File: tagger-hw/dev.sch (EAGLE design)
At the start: 50 parts, among them J2 22-23-2021, J3 22-23-2021, X1 EXC-31B

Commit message: Fix some package sizes (0805 -> 0603)
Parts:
- ACT, PGOOD, USBACT: device adafruit:LEDCHIP-LED0805 -> adafruit:LEDCHIP-LED0603
- R1, R12, R13: device adafruit:R-US_R0805 -> adafruit:R-US_R0603
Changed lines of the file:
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@@
 <grid distance="0.1" unitdist="inch" unit="inch" style="lines" multiple="1" display="no" altdistance="0.01" altunitdist="inch" altunit="inch"/>
 <layers>
-<layer number="1" name="Top" color="4" fill="1" visible="no" active="no"/>
-<layer number="16" name="Bottom" color="1" fill="1" visible="no" active="no"/>
-<layer number="17" name="Pads" color="2" fill="1" visible="no" active="no"/>
-<layer number="18" name="Vias" color="2" fill="1" visible="no" active="no"/>
-<layer number="19" name="Unrouted" color="6" fill="1" visible="no" active="no"/>
-<layer number="20" name="Dimension" color="24" fill="1" visible="no" active="no"/>
-<layer number="21" name="tPlace" color="7" fill="1" visible="no" active="no"/>
-<layer number="22" name="bPlace" color="7" fill="1" visible="no" active="no"/>
-<layer number="23" name="tOrigins" color="15" fill="1" visible="no" active="no"/>
-<layer number="24" name="bOrigins" color="15" fill="1" visible="no" active="no"/>
-<layer number="25" name="tNames" color="7" fill="1" visible="no" active="no"/>
-<layer number="26" name="bNames" color="7" fill="1" visible="no" active="no"/>
-<layer number="27" name="tValues" color="7" fill="1" visible="no" active="no"/>
-<layer number="28" name="bValues" color="7" fill="1" visible="no" active="no"/>
+<layer number="1" name="Top" color="4" fill="1" visible="yes" active="no"/>
+<layer number="16" name="Bottom" color="1" fill="1" visible="yes" active="no"/>
+<layer number="17" name="Pads" color="2" fill="1" visible="yes" active="no"/>
+<layer number="18" name="Vias" color="2" fill="1" visible="yes" active="no"/>
+<layer number="19" name="Unrouted" color="6" fill="1" visible="yes" active="no"/>
+<layer number="20" name="Dimension" color="24" fill="1" visible="yes" active="no"/>
+<layer number="21" name="tPlace" color="7" fill="1" visible="yes" active="no"/>
+<layer number="22" name="bPlace" color="7" fill="1" visible="yes" active="no"/>
+<layer number="23" name="tOrigins" color="15" fill="1" visible="yes" active="no"/>
+<layer number="24" name="bOrigins" color="15" fill="1" visible="yes" active="no"/>
+<layer number="25" name="tNames" color="7" fill="1" visible="yes" active="no"/>
+<layer number="26" name="bNames" color="7" fill="1" visible="yes" active="no"/>
+<layer number="27" name="tValues" color="7" fill="1" visible="yes" active="no"/>
+<layer number="28" name="bValues" color="7" fill="1" visible="yes" active="no"/>
 <layer number="29" name="tStop" color="7" fill="3" visible="no" active="no"/>
 <layer number="30" name="bStop" color="7" fill="6" visible="no" active="no"/>
@@
 <layer number="35" name="tGlue" color="7" fill="4" visible="no" active="no"/>
 <layer number="36" name="bGlue" color="7" fill="5" visible="no" active="no"/>
-<layer number="37" name="tTest" color="7" fill="1" visible="no" active="no"/>
-<layer number="38" name="bTest" color="7" fill="1" visible="no" active="no"/>
+<layer number="37" name="tTest" color="7" fill="1" visible="yes" active="no"/>
+<layer number="38" name="bTest" color="7" fill="1" visible="yes" active="no"/>
 <layer number="39" name="tKeepout" color="4" fill="11" visible="no" active="no"/>
 <layer number="40" name="bKeepout" color="1" fill="11" visible="no" active="no"/>
@@
 <layer number="44" name="Drills" color="7" fill="1" visible="no" active="no"/>
 <layer number="45" name="Holes" color="7" fill="1" visible="no" active="no"/>
-<layer number="46" name="Milling" color="3" fill="1" visible="no" active="no"/>
-<layer number="47" name="Measures" color="7" fill="1" visible="no" active="no"/>
-<layer number="48" name="Document" color="7" fill="1" visible="no" active="no"/>
-<layer number="49" name="Reference" color="7" fill="1" visible="no" active="no"/>
-<layer number="50" name="dxf" color="7" fill="1" visible="no" active="no"/>
-<layer number="51" name="tDocu" color="7" fill="1" visible="no" active="no"/>
-<layer number="52" name="bDocu" color="7" fill="1" visible="no" active="no"/>
-<layer number="53" name="tGND_GNDA" color="7" fill="9" visible="no" active="no"/>
-<layer number="54" name="bGND_GNDA" color="1" fill="9" visible="no" active="no"/>
-<layer number="56" name="wert" color="7" fill="1" visible="no" active="no"/>
-<layer number="57" name="tCAD" color="7" fill="1" visible="no" active="no"/>
-<layer number="59" name="tCarbon" color="7" fill="1" visible="no" active="no"/>
-<layer number="60" name="bCarbon" color="7" fill="1" visible="no" active="no"/>
+<layer number="46" name="Milling" color="3" fill="1" visible="yes" active="no"/>
+<layer number="47" name="Measures" color="7" fill="1" visible="yes" active="no"/>
+<layer number="48" name="Document" color="7" fill="1" visible="yes" active="no"/>
+<layer number="49" name="Reference" color="7" fill="1" visible="yes" active="no"/>
+<layer number="50" name="dxf" color="7" fill="1" visible="yes" active="no"/>
+<layer number="51" name="tDocu" color="7" fill="1" visible="yes" active="no"/>
+<layer number="52" name="bDocu" color="7" fill="1" visible="yes" active="no"/>
+<layer number="53" name="tGND_GNDA" color="7" fill="9" visible="yes" active="no"/>
+<layer number="54" name="bGND_GNDA" color="1" fill="9" visible="yes" active="no"/>
+<layer number="56" name="wert" color="7" fill="1" visible="yes" active="no"/>
+<layer number="57" name="tCAD" color="7" fill="1" visible="yes" active="no"/>
+<layer number="59" name="tCarbon" color="7" fill="1" visible="yes" active="no"/>
+<layer number="60" name="bCarbon" color="7" fill="1" visible="yes" active="no"/>
 <layer number="88" name="SimResults" color="9" fill="1" visible="yes" active="yes"/>
 <layer number="89" name="SimProbes" color="9" fill="1" visible="yes" active="yes"/>
@@
 <part name="SUPPLY4" library="supply2" library_urn="urn:adsk.eagle:library:372" deviceset="GND" device=""/>
 <part name="SUPPLY8" library="supply2" library_urn="urn:adsk.eagle:library:372" deviceset="GND" device=""/>
-<part name="ACT" library="adafruit" deviceset="LED" device="CHIP-LED0805" value="RED"/>
-<part name="R1" library="adafruit" deviceset="R-US_" device="R0805" value="1K"/>
+<part name="ACT" library="adafruit" deviceset="LED" device="CHIP-LED0603" value="RED"/>
+<part name="R1" library="adafruit" deviceset="R-US_" device="R0603" value="1K"/>
 <part name="BUF" library="40xx" library_urn="urn:adsk.eagle:library:80" deviceset="4010" device="D" package3d_urn="urn:adsk.eagle:package:821/2"/>
 <part name="UC" library="adafruit" deviceset="ATMEGA32U4" device="-AU"/>
@@
 <part name="RST" library="switch-omron" library_urn="urn:adsk.eagle:library:377" deviceset="10-XX" device="" package3d_urn="urn:adsk.eagle:package:27496/1" value="B3F-1002"/>
 <part name="S2" library="switch-omron" library_urn="urn:adsk.eagle:library:377" deviceset="10-XX" device="" package3d_urn="urn:adsk.eagle:package:27496/1" value="B3F-1002"/>
-<part name="PGOOD" library="adafruit" deviceset="LED" device="CHIP-LED0805" value="GREEN"/>
-<part name="R12" library="adafruit" deviceset="R-US_" device="R0805" value="1K"/>
+<part name="PGOOD" library="adafruit" deviceset="LED" device="CHIP-LED0603" value="GREEN"/>
+<part name="R12" library="adafruit" deviceset="R-US_" device="R0603" value="1K"/>
 <part name="SUPPLY27" library="supply2" library_urn="urn:adsk.eagle:library:372" deviceset="GND" device=""/>
-<part name="USBACT" library="adafruit" deviceset="LED" device="CHIP-LED0805" value="GREEN"/>
-<part name="R13" library="adafruit" deviceset="R-US_" device="R0805" value="1K"/>
+<part name="USBACT" library="adafruit" deviceset="LED" device="CHIP-LED0603" value="GREEN"/>
+<part name="R13" library="adafruit" deviceset="R-US_" device="R0603" value="1K"/>
 <part name="SUPPLY28" library="supply2" library_urn="urn:adsk.eagle:library:372" deviceset="GND" device=""/>
 <part name="R14" library="resistor" library_urn="urn:adsk.eagle:library:348" deviceset="R-US_" device="R0603" package3d_urn="urn:adsk.eagle:package:26057/1" value="10k"/>

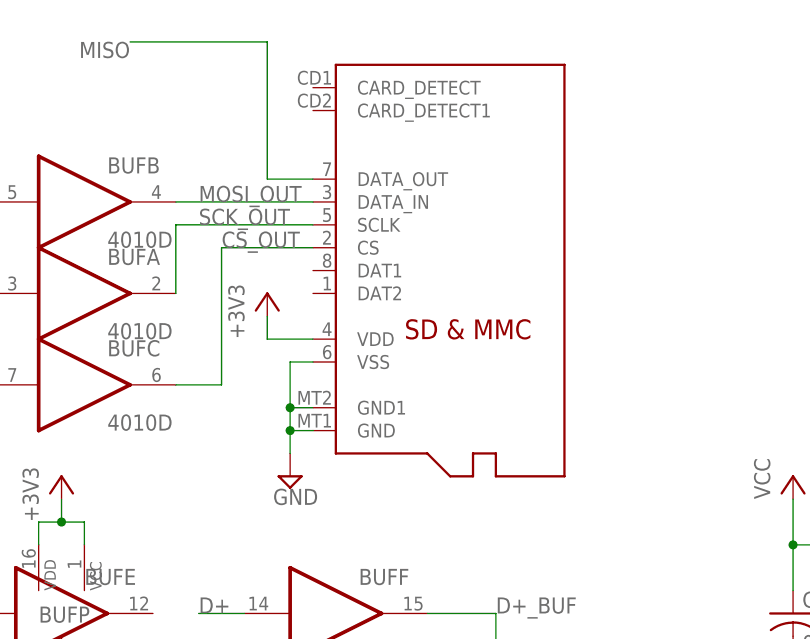
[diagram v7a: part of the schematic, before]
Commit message: New microSD slot pattern
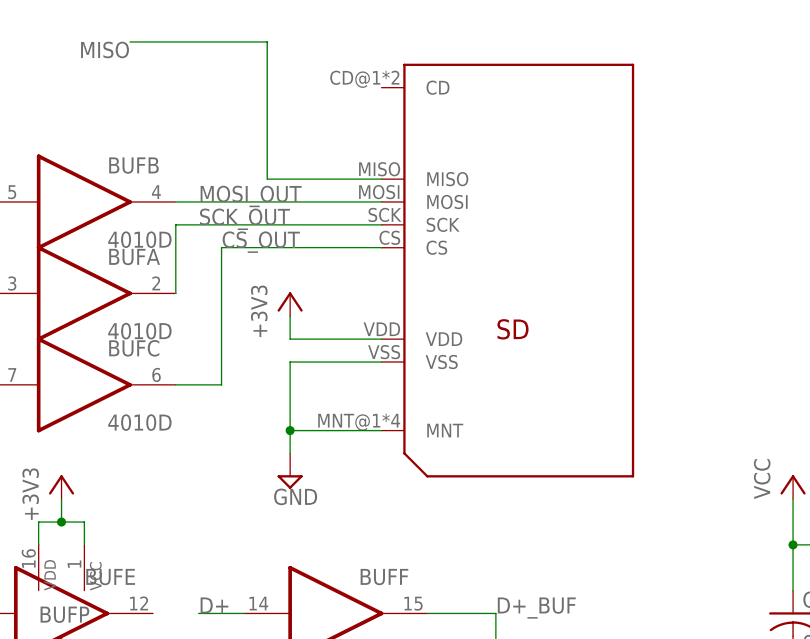
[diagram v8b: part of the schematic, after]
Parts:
- removed SD: MICROSD, adafruit:MICROSD
- added U$1: MICROSD, dorskyee:MICROSD
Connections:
- net +3V3: now also U$1.VDD; no longer SD.VDD
- net CS_OUT: now also U$1.CS; no longer SD.CS
- net GND: now also U$1.MNT, U$1.VSS; no longer SD.GND, SD.GND1, SD.VSS
- net MISO: now also U$1.MISO; no longer SD.DATA_OUT
- net MOSI_OUT: now also U$1.MOSI; no longer SD.DATA_IN
- net SCK_OUT: now also U$1.SCK; no longer SD.SCLK
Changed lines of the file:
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@@
 </classes>
 <parts>
-<part name="SD" library="adafruit" deviceset="MICROSD" device=""/>
 <part name="+3V1" library="supply1" library_urn="urn:adsk.eagle:library:371" deviceset="+3V3" device=""/>
 <part name="+3V2" library="supply1" library_urn="urn:adsk.eagle:library:371" deviceset="+3V3" device=""/>
@@
 <part name="SUPPLY30" library="supply2" library_urn="urn:adsk.eagle:library:372" deviceset="GND" device=""/>
 <part name="+3V15" library="supply1" library_urn="urn:adsk.eagle:library:371" deviceset="+3V3" device=""/>
+<part name="U$1" library="dorskyee" deviceset="MICROSD" device=""/>
 </parts>
 <sheets>
@@
 </plain>
 <instances>
-<instance part="SD" gate="G$1" x="63.5" y="76.2"/>
 <instance part="+3V1" gate="G$1" x="149.86" y="53.34"/>
-<instance part="+3V2" gate="G$1" x="40.64" y="71.12"/>
+<instance part="+3V2" gate="G$1" x="43.18" y="71.12"/>
 <instance part="SUPPLY2" gate="GND" x="43.18" y="50.8"/>
 <instance part="SUPPLY3" gate="GND" x="17.78" y="25.4"/>
@@
 <instance part="SUPPLY30" gate="GND" x="22.86" y="-154.94"/>
 <instance part="+3V15" gate="G$1" x="22.86" y="-114.3"/>
+<instance part="U$1" gate="G$1" x="66.04" y="73.66"/>
 </instances>
 <busses>
@@
 <nets>
 <net name="+3V3" class="0">
-<segment>
-<wire x1="40.64" y1="68.58" x2="40.64" y2="66.04" width="0.1524" layer="91"/>
-<pinref part="+3V2" gate="G$1" pin="+3V3"/>
-<pinref part="SD" gate="G$1" pin="VDD"/>
-<wire x1="45.72" y1="66.04" x2="40.64" y2="66.04" width="0.1524" layer="91"/>
-</segment>
 <segment>
 <wire x1="149.86" y1="50.8" x2="149.86" y2="45.72" width="0.1524" layer="91"/>
@@
 <pinref part="+3V15" gate="G$1" pin="+3V3"/>
 </segment>
+<segment>
+<wire x1="43.18" y1="68.58" x2="43.18" y2="66.04" width="0.1524" layer="91"/>
+<pinref part="+3V2" gate="G$1" pin="+3V3"/>
+<pinref part="U$1" gate="G$1" pin="VDD"/>
+<wire x1="43.18" y1="66.04" x2="53.34" y2="66.04" width="0.1524" layer="91"/>
+</segment>
 </net>
 <net name="GND" class="0">
@@
 <pinref part="SUPPLY13" gate="GND" pin="GND"/>
 <wire x1="-22.86" y1="-12.7" x2="-22.86" y2="-10.16" width="0.1524" layer="91"/>
-</segment>
-<segment>
-<pinref part="SUPPLY2" gate="GND" pin="GND"/>
-<wire x1="43.18" y1="63.5" x2="43.18" y2="58.42" width="0.1524" layer="91"/>
-<pinref part="SD" gate="G$1" pin="VSS"/>
-<wire x1="43.18" y1="58.42" x2="43.18" y2="55.88" width="0.1524" layer="91"/>
-<wire x1="43.18" y1="55.88" x2="43.18" y2="53.34" width="0.1524" layer="91"/>
-<wire x1="45.72" y1="63.5" x2="43.18" y2="63.5" width="0.1524" layer="91"/>
-<pinref part="SD" gate="G$1" pin="GND1"/>
-<wire x1="45.72" y1="58.42" x2="43.18" y2="58.42" width="0.1524" layer="91"/>
-<junction x="43.18" y="58.42"/>
-<pinref part="SD" gate="G$1" pin="GND"/>
-<wire x1="45.72" y1="55.88" x2="43.18" y2="55.88" width="0.1524" layer="91"/>
-<junction x="43.18" y="55.88"/>
 </segment>
 <segment>
@@
 <junction x="22.86" y="-149.86"/>
 </segment>
+<segment>
+<pinref part="SUPPLY2" gate="GND" pin="GND"/>
+<wire x1="43.18" y1="63.5" x2="43.18" y2="55.88" width="0.1524" layer="91"/>
+<pinref part="U$1" gate="G$1" pin="VSS"/>
+<wire x1="43.18" y1="55.88" x2="43.18" y2="53.34" width="0.1524" layer="91"/>
+<wire x1="43.18" y1="63.5" x2="53.34" y2="63.5" width="0.1524" layer="91"/>
+<pinref part="U$1" gate="G$1" pin="MNT"/>
+<wire x1="53.34" y1="55.88" x2="43.18" y2="55.88" width="0.1524" layer="91"/>
+<junction x="43.18" y="55.88"/>
+</segment>
 </net>
 <net name="VCC" class="0">
@@
 <net name="MISO" class="0">
 <segment>
-<wire x1="45.72" y1="83.82" x2="40.64" y2="83.82" width="0.1524" layer="91"/>
+<wire x1="53.34" y1="83.82" x2="40.64" y2="83.82" width="0.1524" layer="91"/>
 <wire x1="40.64" y1="83.82" x2="40.64" y2="99.06" width="0.1524" layer="91"/>
 <wire x1="25.4" y1="99.06" x2="40.64" y2="99.06" width="0.1524" layer="91"/>
 <label x="25.4" y="99.06" size="1.778" layer="95" rot="R180"/>
-<pinref part="SD" gate="G$1" pin="DATA_OUT"/>
+<pinref part="U$1" gate="G$1" pin="MISO"/>
 </segment>
 <segment>
@@
 <net name="MOSI_OUT" class="0">
 <segment>
-<pinref part="SD" gate="G$1" pin="DATA_IN"/>
 <label x="33.02" y="81.28" size="1.778" layer="95"/>
-<wire x1="30.48" y1="81.28" x2="45.72" y2="81.28" width="0.1524" layer="91"/>
+<wire x1="30.48" y1="81.28" x2="53.34" y2="81.28" width="0.1524" layer="91"/>
 <pinref part="BUF" gate="B" pin="O"/>
+<pinref part="U$1" gate="G$1" pin="MOSI"/>
 </segment>
 <segment>
@@
 <net name="SCK_OUT" class="0">
 <segment>
-<wire x1="30.48" y1="78.74" x2="45.72" y2="78.74" width="0.1524" layer="91"/>
-<pinref part="SD" gate="G$1" pin="SCLK"/>
+<wire x1="30.48" y1="78.74" x2="53.34" y2="78.74" width="0.1524" layer="91"/>
 <label x="33.02" y="78.74" size="1.778" layer="95"/>
 <pinref part="BUF" gate="A" pin="O"/>
 <wire x1="30.48" y1="71.12" x2="30.48" y2="78.74" width="0.1524" layer="91"/>
+<pinref part="U$1" gate="G$1" pin="SCK"/>
 </segment>
 <segment>
@@
 <net name="CS_OUT" class="0">
 <segment>
-<pinref part="SD" gate="G$1" pin="CS"/>
-<wire x1="35.56" y1="76.2" x2="45.72" y2="76.2" width="0.1524" layer="91"/>
+<wire x1="35.56" y1="76.2" x2="53.34" y2="76.2" width="0.1524" layer="91"/>
 <wire x1="35.56" y1="60.96" x2="35.56" y2="76.2" width="0.1524" layer="91"/>
 <wire x1="30.48" y1="60.96" x2="35.56" y2="60.96" width="0.1524" layer="91"/>
 <pinref part="BUF" gate="C" pin="O"/>
 <label x="35.56" y="76.2" size="1.778" layer="95"/>
-</segment>
-<segment>
+<pinref part="U$1" gate="G$1" pin="CS"/>
+</segment>
+<segment>
